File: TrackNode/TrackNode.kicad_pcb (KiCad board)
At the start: 2 copper layers, 15 x 15 mm, 15 parts, among them J1 Conn_01x04, J2 Conn_01x02, U1 TLV493D-A1B6, U2 LIS2DTW12

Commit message: Finalized CAD files and configurations
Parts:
- removed C2, C3: 0.1uF, Capacitor_SMD:C_0402_1005Metric
- removed R6, R7: 100, Resistor_SMD:R_0402_1005Metric
- removed U2: LIS2DTW12, Package_LGA:LGA-12_2x2mm_P0.5mm
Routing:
- net /VCC: track 29.8 -> 19.2 mm
- net GND: track 13.1 -> 6.22 mm, vias 6 -> 5
- net Net-(U2-SCL/SPC): track 3.72 -> 0.00 mm
- net Net-(U2-SDA/SDI/SDO): track 3.03 -> 0.00 mm
- net /SCL: track 7.58 -> 5.18 mm
- net /SDA: track 10.9 -> 8.54 mm

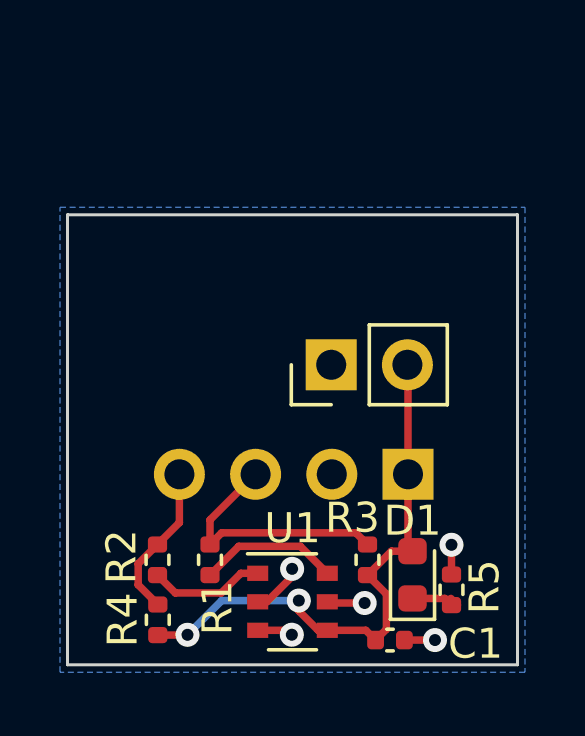
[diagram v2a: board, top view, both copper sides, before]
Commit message: Fixed direction of TrackNode pin header
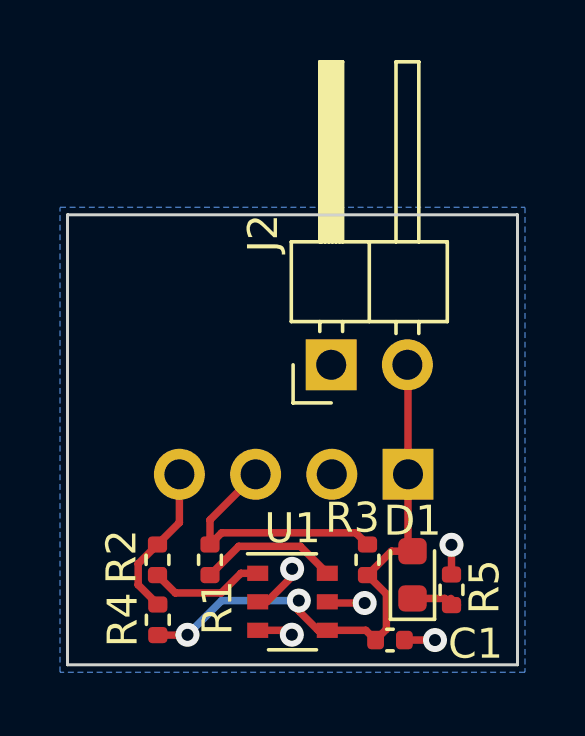
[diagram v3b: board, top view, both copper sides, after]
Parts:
- J2: footprint Connector_PinHeader_2.54mm:PinHeader_1x02_P2.54mm_Vertical -> Connector_PinHeader_2.54mm:PinHeader_1x02_P2.54mm_Horizontal
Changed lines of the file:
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@@
     )
   )
-  (footprint "Connector_PinHeader_2.54mm:PinHeader_1x02_P2.54mm_Vertical" (layer "F.Cu")
+  (footprint "Connector_PinHeader_2.54mm:PinHeader_1x02_P2.54mm_Horizontal" (layer "F.Cu")
     (at 27.29 25 90)
-    (descr "Through hole straight pin header, 1x02, 2.54mm pitch, single row")
-    (tags "Through hole pin header THT 1x02 2.54mm single row")
+    (descr "Through hole angled pin header, 1x02, 2.54mm pitch, 6mm pin length, single row")
+    (tags "Through hole angled pin header THT 1x02 2.54mm single row")
     (property "Sheetfile" "TrackNode.kicad_sch")
     (property "Sheetname" "")
@@
     (property "ki_keywords" "connector")
     (attr through_hole)
-    (fp_text reference "J2" (at -1.6 -1.29 90) (layer "F.SilkS") hide
+    (fp_text reference "J2" (at 4.385 -2.27 90) (layer "F.SilkS")
         (effects (font (size 1 1) (thickness 0.15)))
     )
-    (fp_text value "Conn_01x02" (at 0 4.87 90) (layer "F.Fab")
+    (fp_text value "Conn_01x02" (at 4.385 4.81 90) (layer "F.Fab")
         (effects (font (size 1 1) (thickness 0.15)))
     )
-    (fp_text user "${REFERENCE}" (at 0 1.27) (layer "F.Fab")
+    (fp_text user "${REFERENCE}" (at 2.77 1.27 180) (layer "F.Fab")
         (effects (font (size 1 1) (thickness 0.15)))
     )
-    (fp_line (start -1.33 -1.33) (end 0 -1.33)
+    (fp_line (start -1.27 -1.27) (end 0 -1.27)
       (stroke (width 0.12) (type solid)) (layer "F.SilkS"))
-    (fp_line (start -1.33 0) (end -1.33 -1.33)
+    (fp_line (start -1.27 0) (end -1.27 -1.27)
       (stroke (width 0.12) (type solid)) (layer "F.SilkS"))
-    (fp_line (start -1.33 1.27) (end -1.33 3.87)
+    (fp_line (start 1.042929 2.16) (end 1.44 2.16)
       (stroke (width 0.12) (type solid)) (layer "F.SilkS"))
-    (fp_line (start -1.33 1.27) (end 1.33 1.27)
+    (fp_line (start 1.042929 2.92) (end 1.44 2.92)
       (stroke (width 0.12) (type solid)) (layer "F.SilkS"))
-    (fp_line (start -1.33 3.87) (end 1.33 3.87)
+    (fp_line (start 1.11 -0.38) (end 1.44 -0.38)
       (stroke (width 0.12) (type solid)) (layer "F.SilkS"))
-    (fp_line (start 1.33 1.27) (end 1.33 3.87)
+    (fp_line (start 1.11 0.38) (end 1.44 0.38)
+      (stroke (width 0.12) (type solid)) (layer "F.SilkS"))
+    (fp_line (start 1.44 -1.33) (end 1.44 3.87)
+      (stroke (width 0.12) (type solid)) (layer "F.SilkS"))
+    (fp_line (start 1.44 1.27) (end 4.1 1.27)
+      (stroke (width 0.12) (type solid)) (layer "F.SilkS"))
+    (fp_line (start 1.44 3.87) (end 4.1 3.87)
+      (stroke (width 0.12) (type solid)) (layer "F.SilkS"))
+    (fp_line (start 4.1 -1.33) (end 1.44 -1.33)
+      (stroke (width 0.12) (type solid)) (layer "F.SilkS"))
+    (fp_line (start 4.1 -0.38) (end 10.1 -0.38)
+      (stroke (width 0.12) (type solid)) (layer "F.SilkS"))
+    (fp_line (start 4.1 -0.32) (end 10.1 -0.32)
+      (stroke (width 0.12) (type solid)) (layer "F.SilkS"))
+    (fp_line (start 4.1 -0.2) (end 10.1 -0.2)
+      (stroke (width 0.12) (type solid)) (layer "F.SilkS"))
+    (fp_line (start 4.1 -0.08) (end 10.1 -0.08)
+      (stroke (width 0.12) (type solid)) (layer "F.SilkS"))
+    (fp_line (start 4.1 0.04) (end 10.1 0.04)
+      (stroke (width 0.12) (type solid)) (layer "F.SilkS"))
+    (fp_line (start 4.1 0.16) (end 10.1 0.16)
+      (stroke (width 0.12) (type solid)) (layer "F.SilkS"))
+    (fp_line (start 4.1 0.28) (end 10.1 0.28)
+      (stroke (width 0.12) (type solid)) (layer "F.SilkS"))
+    (fp_line (start 4.1 2.16) (end 10.1 2.16)
+      (stroke (width 0.12) (type solid)) (layer "F.SilkS"))
+    (fp_line (start 4.1 3.87) (end 4.1 -1.33)
+      (stroke (width 0.12) (type solid)) (layer "F.SilkS"))
+    (fp_line (start 10.1 -0.38) (end 10.1 0.38)
+      (stroke (width 0.12) (type solid)) (layer "F.SilkS"))
+    (fp_line (start 10.1 0.38) (end 4.1 0.38)
+      (stroke (width 0.12) (type solid)) (layer "F.SilkS"))
+    (fp_line (start 10.1 2.16) (end 10.1 2.92)
+      (stroke (width 0.12) (type solid)) (layer "F.SilkS"))
+    (fp_line (start 10.1 2.92) (end 4.1 2.92)
       (stroke (width 0.12) (type solid)) (layer "F.SilkS"))
     (fp_line (start -1.8 -1.8) (end -1.8 4.35)
       (stroke (width 0.05) (type solid)) (layer "F.CrtYd"))
-    (fp_line (start -1.8 4.35) (end 1.8 4.35)
+    (fp_line (start -1.8 4.35) (end 10.55 4.35)
       (stroke (width 0.05) (type solid)) (layer "F.CrtYd"))
-    (fp_line (start 1.8 -1.8) (end -1.8 -1.8)
+    (fp_line (start 10.55 -1.8) (end -1.8 -1.8)
       (stroke (width 0.05) (type solid)) (layer "F.CrtYd"))
-    (fp_line (start 1.8 4.35) (end 1.8 -1.8)
+    (fp_line (start 10.55 4.35) (end 10.55 -1.8)
       (stroke (width 0.05) (type solid)) (layer "F.CrtYd"))
-    (fp_line (start -1.27 -0.635) (end -0.635 -1.27)
+    (fp_line (start -0.32 -0.32) (end -0.32 0.32)
       (stroke (width 0.1) (type solid)) (layer "F.Fab"))
-    (fp_line (start -1.27 3.81) (end -1.27 -0.635)
+    (fp_line (start -0.32 -0.32) (end 1.5 -0.32)
       (stroke (width 0.1) (type solid)) (layer "F.Fab"))
-    (fp_line (start -0.635 -1.27) (end 1.27 -1.27)
+    (fp_line (start -0.32 0.32) (end 1.5 0.32)
       (stroke (width 0.1) (type solid)) (layer "F.Fab"))
-    (fp_line (start 1.27 -1.27) (end 1.27 3.81)
+    (fp_line (start -0.32 2.22) (end -0.32 2.86)
       (stroke (width 0.1) (type solid)) (layer "F.Fab"))
-    (fp_line (start 1.27 3.81) (end -1.27 3.81)
+    (fp_line (start -0.32 2.22) (end 1.5 2.22)
+      (stroke (width 0.1) (type solid)) (layer "F.Fab"))
+    (fp_line (start -0.32 2.86) (end 1.5 2.86)
+      (stroke (width 0.1) (type solid)) (layer "F.Fab"))
+    (fp_line (start 1.5 -0.635) (end 2.135 -1.27)
+      (stroke (width 0.1) (type solid)) (layer "F.Fab"))
+    (fp_line (start 1.5 3.81) (end 1.5 -0.635)
+      (stroke (width 0.1) (type solid)) (layer "F.Fab"))
+    (fp_line (start 2.135 -1.27) (end 4.04 -1.27)
+      (stroke (width 0.1) (type solid)) (layer "F.Fab"))
+    (fp_line (start 4.04 -1.27) (end 4.04 3.81)
+      (stroke (width 0.1) (type solid)) (layer "F.Fab"))
+    (fp_line (start 4.04 -0.32) (end 10.04 -0.32)
+      (stroke (width 0.1) (type solid)) (layer "F.Fab"))
+    (fp_line (start 4.04 0.32) (end 10.04 0.32)
+      (stroke (width 0.1) (type solid)) (layer "F.Fab"))
+    (fp_line (start 4.04 2.22) (end 10.04 2.22)
+      (stroke (width 0.1) (type solid)) (layer "F.Fab"))
+    (fp_line (start 4.04 2.86) (end 10.04 2.86)
+      (stroke (width 0.1) (type solid)) (layer "F.Fab"))
+    (fp_line (start 4.04 3.81) (end 1.5 3.81)
+      (stroke (width 0.1) (type solid)) (layer "F.Fab"))
+    (fp_line (start 10.04 -0.32) (end 10.04 0.32)
+      (stroke (width 0.1) (type solid)) (layer "F.Fab"))
+    (fp_line (start 10.04 2.22) (end 10.04 2.86)
       (stroke (width 0.1) (type solid)) (layer "F.Fab"))
     (pad "1" thru_hole rect (at 0 0 90) (size 1.7 1.7) (drill 1) (layers "*.Cu" "*.Mask")
@@
     (pad "2" thru_hole oval (at 0 2.54 90) (size 1.7 1.7) (drill 1) (layers "*.Cu" "*.Mask")
       (net 1 "/VCC") (pinfunction "Pin_2") (pintype "passive"))
-    (model "${KICAD6_3DMODEL_DIR}/Connector_PinHeader_2.54mm.3dshapes/PinHeader_1x02_P2.54mm_Vertical.wrl"
+    (model "${KICAD6_3DMODEL_DIR}/Connector_PinHeader_2.54mm.3dshapes/PinHeader_1x02_P2.54mm_Horizontal.wrl"
       (offset (xyz 0 0 0))
       (scale (xyz 1 1 1))
